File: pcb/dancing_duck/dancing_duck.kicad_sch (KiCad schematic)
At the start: 9 parts, among them J1 Conn_01x02, J2 Conn_01x02, J3 Conn_01x02, J4 Conn_01x02, J5 Conn_01x02_Pin, J6 Conn_01x01_Pin

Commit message: feat: add battery adc to pcb
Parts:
- added R1: 220k, Resistor_SMD:R_1206_3216Metric_Pad1.30x1.75mm_HandSolder, symbol Device:R_US
- added R2: 330k, Resistor_SMD:R_1206_3216Metric_Pad1.30x1.75mm_HandSolder, symbol Device:R_US
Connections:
- net GND: now also R2.2
- net VCC: now also R1.1
- net at U1.31 (GP26): now also R1.2, R2.1
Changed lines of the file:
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@@
   (junction (at 104.14 121.92) (diameter 0) (color 0 0 0 0)
   )
+  (junction (at 177.8 134.62) (diameter 0) (color 0 0 0 0)
+  )
   (junction (at 104.14 91.44) (diameter 0) (color 0 0 0 0)
   )
@@
     (stroke (width 0) (type default))
   )
+  (wire (pts (xy 100.33 114.3) (xy 170.18 114.3))
+    (stroke (width 0) (type default))
+  )
   (wire (pts (xy 123.19 109.22) (xy 123.19 116.84))
     (stroke (width 0) (type default))
@@
     (stroke (width 0) (type default))
   )
+  (wire (pts (xy 170.18 134.62) (xy 177.8 134.62))
+    (stroke (width 0) (type default))
+  )
+  (wire (pts (xy 177.8 133.35) (xy 177.8 134.62))
+    (stroke (width 0) (type default))
+  )
   (wire (pts (xy 134.62 127) (xy 130.81 127))
     (stroke (width 0) (type default))
@@
     (stroke (width 0) (type default))
   )
+  (wire (pts (xy 170.18 114.3) (xy 170.18 134.62))
+    (stroke (width 0) (type default))
+  )
   (wire (pts (xy 104.14 109.22) (xy 104.14 121.92))
     (stroke (width 0) (type default))
@@
     (stroke (width 0) (type default))
   )
+  (wire (pts (xy 177.8 123.19) (xy 177.8 125.73))
+    (stroke (width 0) (type default))
+  )
   (wire (pts (xy 116.84 67.31) (xy 116.84 73.66))
     (stroke (width 0) (type default))
@@
     (stroke (width 0) (type default))
   )
-  (wire (pts (xy 130.81 124.46) (xy 130.81 116.84))
+  (wire (pts (xy 130.81 124.46) (xy 130.81 121.92))
     (stroke (width 0) (type default))
   )
@@
     (stroke (width 0) (type default))
   )
+  (wire (pts (xy 177.8 134.62) (xy 177.8 135.89))
+    (stroke (width 0) (type default))
+  )
   (wire (pts (xy 50.8 93.98) (xy 69.85 93.98))
     (stroke (width 0) (type default))
@@
     (stroke (width 0) (type default))
   )
+  (wire (pts (xy 177.8 143.51) (xy 177.8 146.05))
+    (stroke (width 0) (type default))
+  )
   (wire (pts (xy 124.46 119.38) (xy 124.46 102.87))
     (stroke (width 0) (type default))
@@
   (wire (pts (xy 118.11 64.77) (xy 118.11 76.2))
     (stroke (width 0) (type default))
-  )
-  (text_box "Todo:\n- Add battery ADC voltage divider\n"
-    (at 101.6 21.59 0) (size 69.85 34.29)
-    (stroke (width 0) (type default))
-    (fill (type color) (color 255 244 0 1))
-    (effects (font (size 1.27 1.27)) (justify left top))
   )
   (netclass_flag "" (length 2.54) (shape round) (at 129.54 85.09 180) (fields_autoplaced)
@@
         (path "/adb842c0-33ba-4e81-bd0d-80db0bf23605"
           (reference "J4") (unit 1)
+        )
+      )
+    )
+  )
+  (symbol (lib_id "Device:R_US") (at 177.8 139.7 0) (unit 1)
+    (in_bom yes) (on_board yes) (dnp no) (fields_autoplaced)
+    (property "Reference" "R2" (at 180.34 138.43 0)
+      (effects (font (size 1.27 1.27)) (justify left))
+    )
+    (property "Value" "330k" (at 180.34 140.97 0)
+      (effects (font (size 1.27 1.27)) (justify left))
+    )
+    (property "Footprint" "Resistor_SMD:R_1206_3216Metric_Pad1.30x1.75mm_HandSolder" (at 178.816 139.954 90)
+      (effects (font (size 1.27 1.27)) hide)
+    )
+    (property "Datasheet" "~" (at 177.8 139.7 0)
+      (effects (font (size 1.27 1.27)) hide)
+    )
+    (pin "2")
+    (pin "1")
+    (instances
+      (project "dancing_duck"
+        (path "/adb842c0-33ba-4e81-bd0d-80db0bf23605"
+          (reference "R2") (unit 1)
+        )
+      )
+    )
+  )
+  (symbol (lib_id "power:GND") (at 177.8 146.05 0) (unit 1)
+    (in_bom yes) (on_board yes) (dnp no) (fields_autoplaced)
+    (property "Reference" "#PWR010" (at 177.8 152.4 0)
+      (effects (font (size 1.27 1.27)) hide)
+    )
+    (property "Value" "GND" (at 177.8 151.13 0)
+      (effects (font (size 1.27 1.27)))
+    )
+    (property "Footprint" "" (at 177.8 146.05 0)
+      (effects (font (size 1.27 1.27)) hide)
+    )
+    (property "Datasheet" "" (at 177.8 146.05 0)
+      (effects (font (size 1.27 1.27)) hide)
+    )
+    (pin "1")
+    (instances
+      (project "dancing_duck"
+        (path "/adb842c0-33ba-4e81-bd0d-80db0bf23605"
+          (reference "#PWR010") (unit 1)
         )
       )
@@
     )
   )
+  (symbol (lib_id "Device:R_US") (at 177.8 129.54 0) (unit 1)
+    (in_bom yes) (on_board yes) (dnp no) (fields_autoplaced)
+    (property "Reference" "R1" (at 180.34 128.27 0)
+      (effects (font (size 1.27 1.27)) (justify left))
+    )
+    (property "Value" "220k" (at 180.34 130.81 0)
+      (effects (font (size 1.27 1.27)) (justify left))
+    )
+    (property "Footprint" "Resistor_SMD:R_1206_3216Metric_Pad1.30x1.75mm_HandSolder" (at 178.816 129.794 90)
+      (effects (font (size 1.27 1.27)) hide)
+    )
+    (property "Datasheet" "~" (at 177.8 129.54 0)
+      (effects (font (size 1.27 1.27)) hide)
+    )
+    (pin "2")
+    (pin "1")
+    (instances
+      (project "dancing_duck"
+        (path "/adb842c0-33ba-4e81-bd0d-80db0bf23605"
+          (reference "R1") (unit 1)
+        )
+      )
+    )
+  )
   (symbol (lib_id "Connector:Conn_01x01_Pin") (at 142.24 109.22 180) (unit 1)
     (in_bom yes) (on_board yes) (dnp no)
@@
     )
   )
-  (symbol (lib_id "power:+3V3") (at 130.81 116.84 0) (unit 1)
+  (symbol (lib_id "power:+3V3") (at 130.81 121.92 0) (unit 1)
     (in_bom yes) (on_board yes) (dnp no)
-    (property "Reference" "#PWR07" (at 130.81 120.65 0)
-      (effects (font (size 1.27 1.27)) hide)
-    )
-    (property "Value" "+3V3" (at 130.81 111.76 0)
-      (effects (font (size 1.27 1.27)))
-    )
-    (property "Footprint" "" (at 130.81 116.84 0)
-      (effects (font (size 1.27 1.27)) hide)
-    )
-    (property "Datasheet" "" (at 130.81 116.84 0)
+    (property "Reference" "#PWR07" (at 130.81 125.73 0)
+      (effects (font (size 1.27 1.27)) hide)
+    )
+    (property "Value" "+3V3" (at 130.81 118.11 0)
+      (effects (font (size 1.27 1.27)))
+    )
+    (property "Footprint" "" (at 130.81 121.92 0)
+      (effects (font (size 1.27 1.27)) hide)
+    )
+    (property "Datasheet" "" (at 130.81 121.92 0)
       (effects (font (size 1.27 1.27)) hide)
     )
@@
         )
       )
+    )
+  )
+  (symbol (lib_id "power:VCC") (at 177.8 123.19 0) (unit 1)
+    (in_bom yes) (on_board yes) (dnp no) (fields_autoplaced)
+    (property "Reference" "#PWR09" (at 177.8 127 0)
+      (effects (font (size 1.27 1.27)) hide)
+    )
+    (property "Value" "VCC" (at 177.8 118.11 0)
+      (effects (font (size 1.27 1.27)))
+    )
+    (property "Footprint" "" (at 177.8 123.19 0)
+      (effects (font (size 1.27 1.27)) hide)
+    )
+    (property "Datasheet" "" (at 177.8 123.19 0)
+      (effects (font (size 1.27 1.27)) hide)
+    )
+    (pin "1")
+    (instances
+      (project "dancing_duck"
+        (path "/adb842c0-33ba-4e81-bd0d-80db0bf23605"
+          (reference "#PWR09") (unit 1)
+        )
+      )

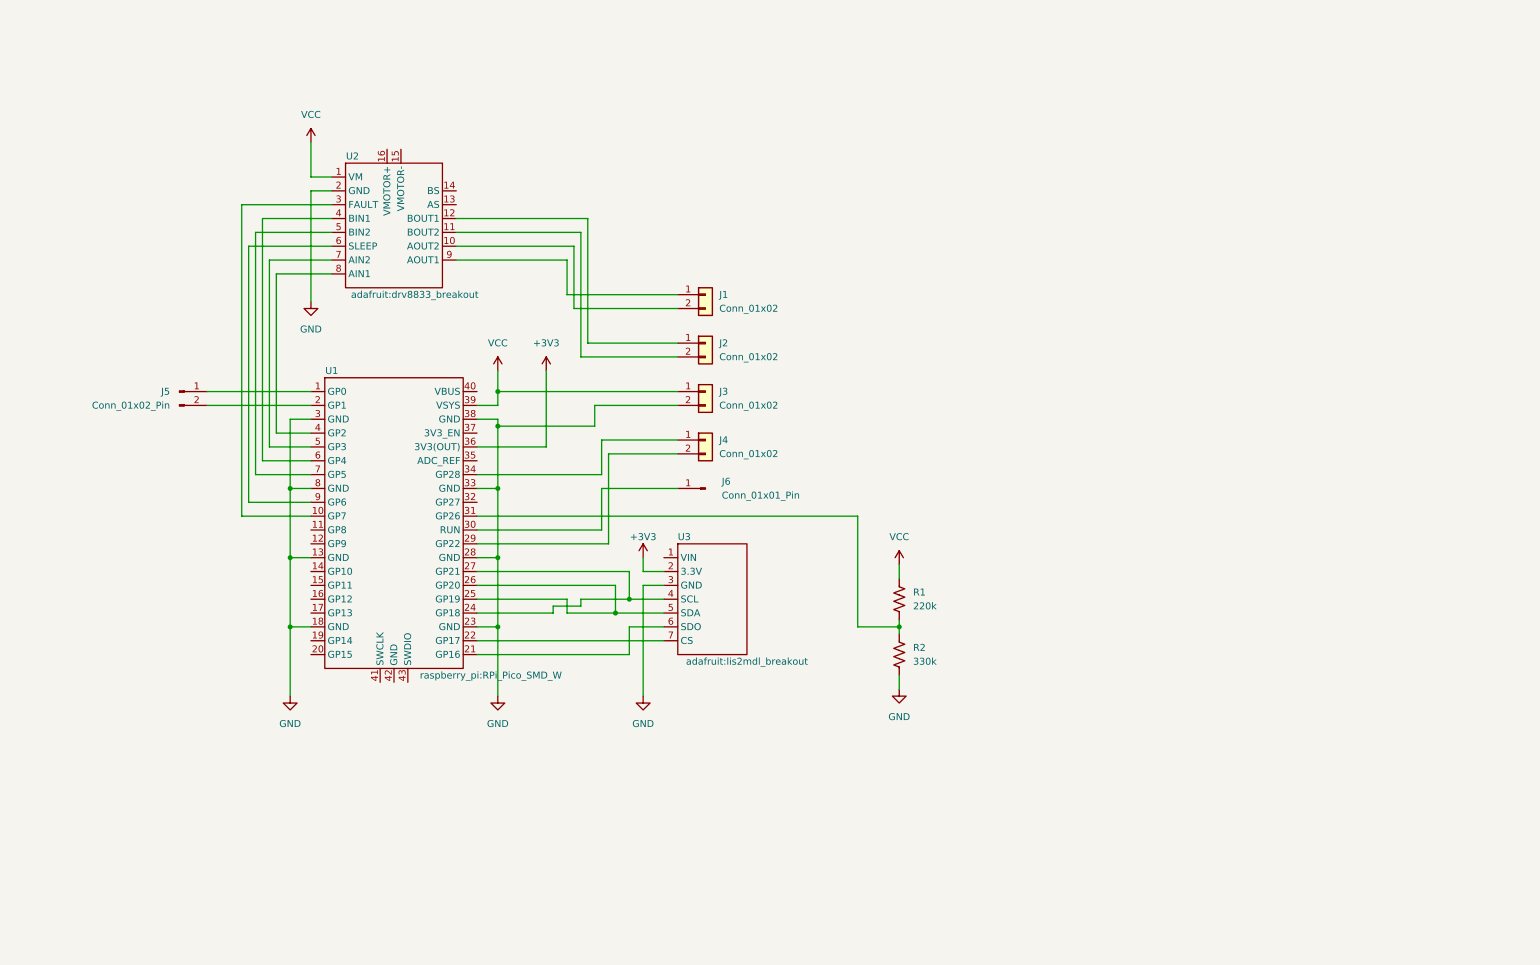
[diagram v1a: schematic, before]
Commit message: doc: update schematic
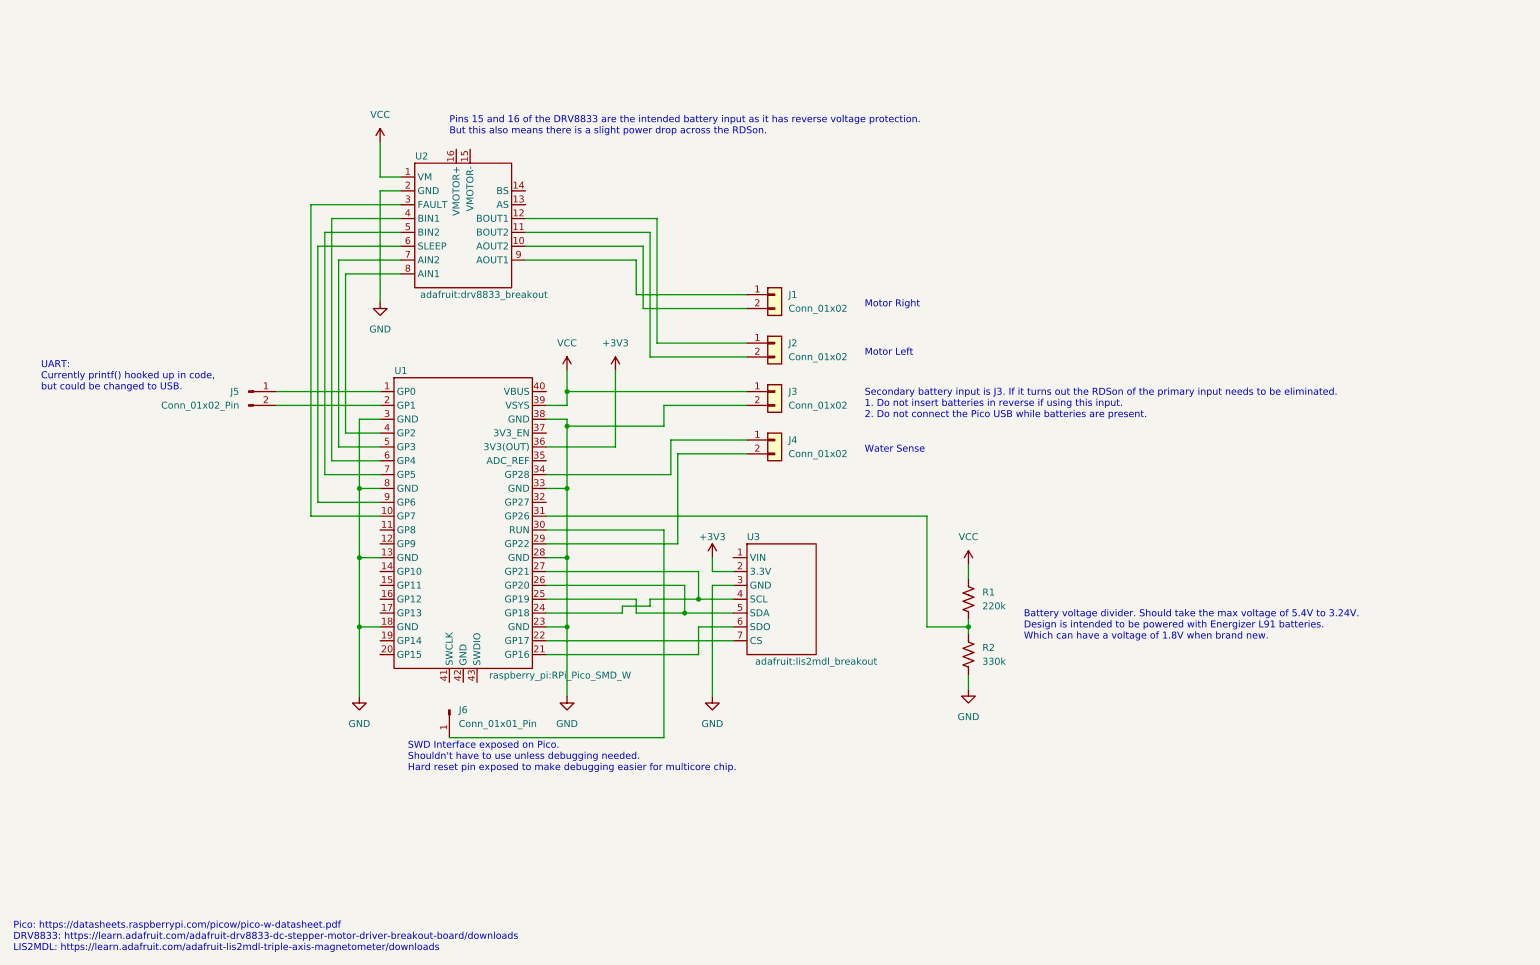
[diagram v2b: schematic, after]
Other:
- note added: "Battery voltage divider. Should take the max voltage of 5.4V to 3.24V. Design is intended to be powered with Energizer L91 batteries. Which can have a voltage of 1.8V when brand new."
- note added: "Motor Left"
- note added: "Motor Right"
- note added: "Pico: https://datasheets.raspberrypi.com/picow/pico-w-datasheet.pdf DRV8833: https://learn.adafruit.com/adafruit-drv8833-dc-stepper-motor-driver-breakout-board/downloads LIS2MDL: https://learn.adafruit.com/adafruit-lis2mdl-triple-axis-magnetometer/downloads"
- note added: "Pins 15 and 16 of the DRV8833 are the intended battery input as it has reverse voltage protection. But this also means there is a slight power drop across the RDSon."
- note added: "SWD Interface exposed on Pico. Shouldn't have to use unless debugging needed. Hard reset pin exposed to make debugging easier for multicore chip."
- note added: "Secondary battery input is J3. If it turns out the RDSon of the primary input needs to be eliminated. 1. Do not insert batteries in reverse if using this input. 2. Do not connect the Pico USB while batteries are present."
- note added: "UART: Currently printf() hooked up in code, but could be changed to USB."
- note added: "Water Sense"
- company: (none) -> Shadow Grove Lab/Seattle Design Nerds
- title: (none) -> Dancing Duck Carrier Board
- moved on the sheet: J1, J2, J3, J4, J5, J6, R1, R2, U1, U2, U3

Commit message: doc: update schematic
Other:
- note added: "SPI and I2C both connected"
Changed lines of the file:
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@@
+    (effects (font (size 1.27 1.27)) (justify left bottom))
+  )
+  (text "SPI and I2C both connected" (at 144.78 144.78 0)
     (effects (font (size 1.27 1.27)) (justify left bottom))
   )
